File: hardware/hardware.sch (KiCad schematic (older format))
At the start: 12 parts

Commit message: wip: power supply
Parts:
- added C? (x3): CP, symbol Device:CP
- added C? (x5): C, symbol Device:C
- added J?: Conn_01x02_Male, symbol Connector:Conn_01x02_Male
- added K?: HE721C0500, DIP952W51P254L1905H550Q14N, symbol HE721C0500:HE721C0500
- added L? (x2): L, symbol Device:L
- added Q?: BC107, Package_TO_SOT_THT:TO-18-3, symbol Transistor_BJT:BC107
- added SW?: Trk next, symbol Switch:SW_Push
- added SW?: Trk prev, symbol Switch:SW_Push
- added SW?: Vol up, symbol Switch:SW_Push
- added SW?: Vol down, symbol Switch:SW_Push
- added SW?: SW_Push, symbol Switch:SW_Push
- added U?: TLV1117-33, symbol Regulator_Linear:TLV1117-33
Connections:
- net labels added: +3.3V, CTS, DTR
- wire segments 90 -> 132
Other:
- moved on the sheet: J?, R?, U?

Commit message: wip: power switch and cleanup
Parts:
- added D? (x2): D, symbol Device:D
- added R? (x2): 10k, symbol Device:R
- J?: value Conn_01x02_Male -> Power
- SW?: value SW_Push -> Power
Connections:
- net labels added: POWER_CTRL, RFID-MISO, RFID-MOSI, RFID-RST, RFID-SCK, RFID-SDA, SD-CS, SD-MISO, SD-MOSI, SD-SCK, SW_POWER, TRK_NEXT, TRK_PREV, VOL_DOWN, VOL_UP
- net labels removed: CS, GND, MISO, MOSI, RST, SDA, VIN
- wire segments 132 -> 116
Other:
- moved on the sheet: C?, J?, K?, Q?, R?, SW?, U?

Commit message: fix power switch circuit
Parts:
- added D? (x4): D, symbol Device:D
- added Q?: BC107, Package_TO_SOT_THT:TO-18-3, symbol Transistor_BJT:BC107
- added R? (x3): 10k, symbol Device:R
- added R?: 220, symbol Device:R
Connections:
- wire segments 116 -> 130
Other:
- moved on the sheet: C?, D?, J?, Q?, R?, SW?, U?

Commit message: update schematics
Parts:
- removed C? (x2): CP, symbol Device:CP
- removed D? (x5): D, symbol Device:D
- removed J?: Power, symbol Connector:Conn_01x02_Male
- removed L?: L, symbol Device:L
- removed Q?: BC107, Package_TO_SOT_THT:TO-18-3, symbol Transistor_BJT:BC107
- removed R? (x5): 10k, symbol Device:R
- removed SW?: Power, symbol Switch:SW_Push
- added C? (x2): 4.7uF, symbol Device:C
- added C?: C, symbol Device:C
- added J?: Power, symbol Connector:Conn_01x03_Male
- added R?: 150k, symbol Device:R
- added R?: 390k, symbol Device:R
- added U?: XRP6272, symbol XRP6272:XRP6272
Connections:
- wire segments 130 -> 123
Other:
- moved on the sheet: Q?, R?

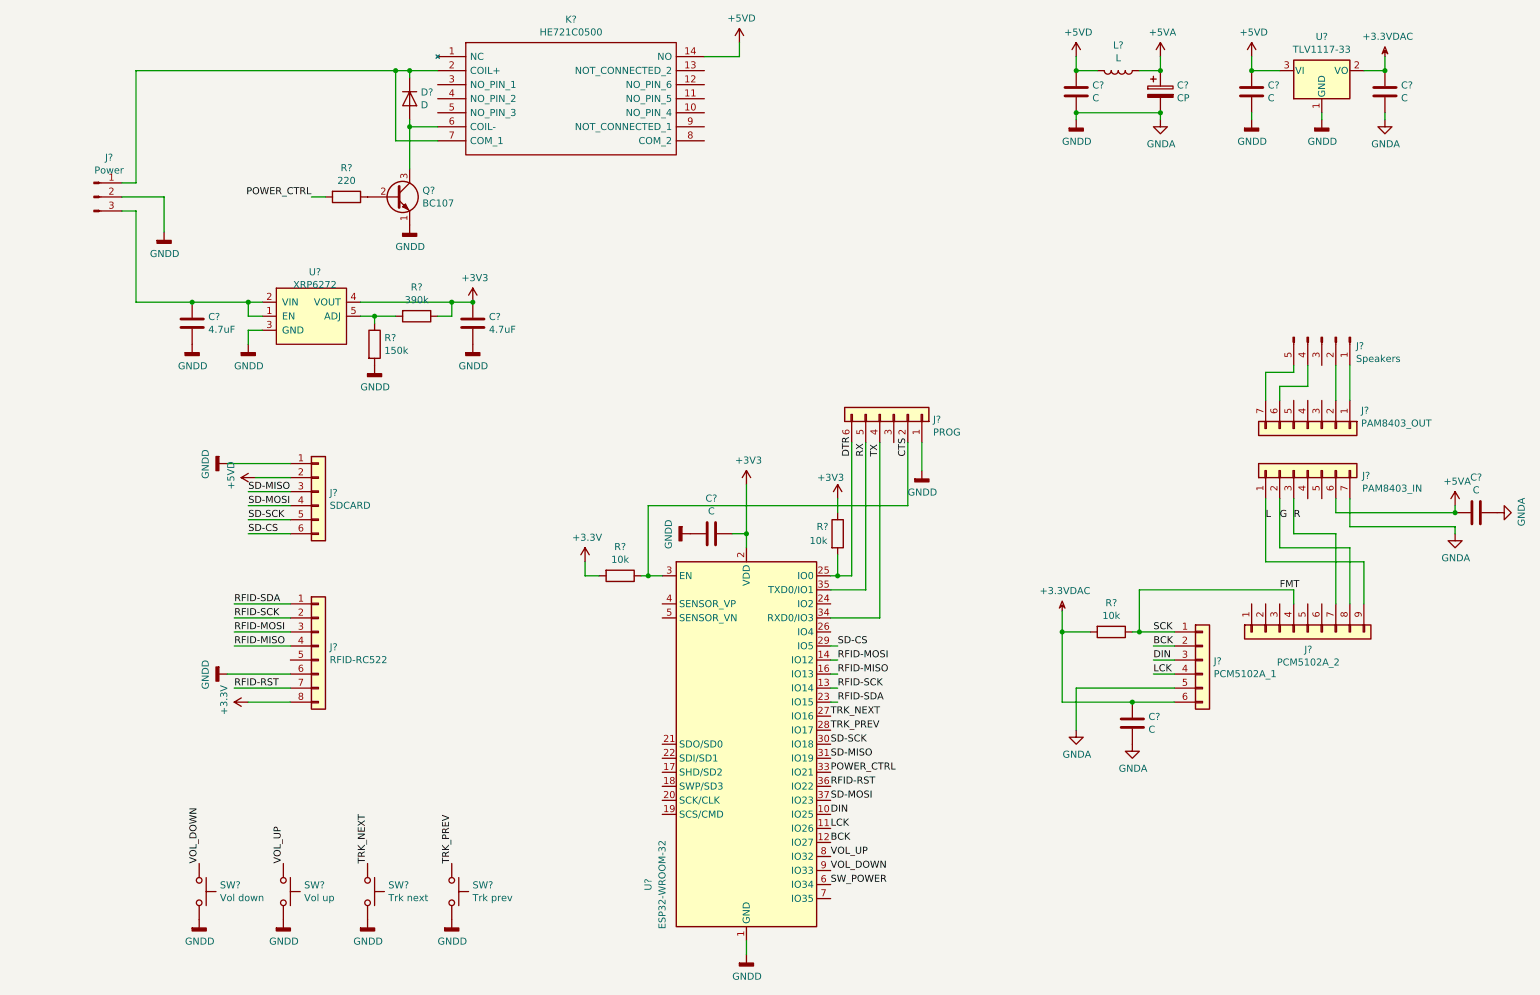
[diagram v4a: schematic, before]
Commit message: update schematics, improve power distribution concept
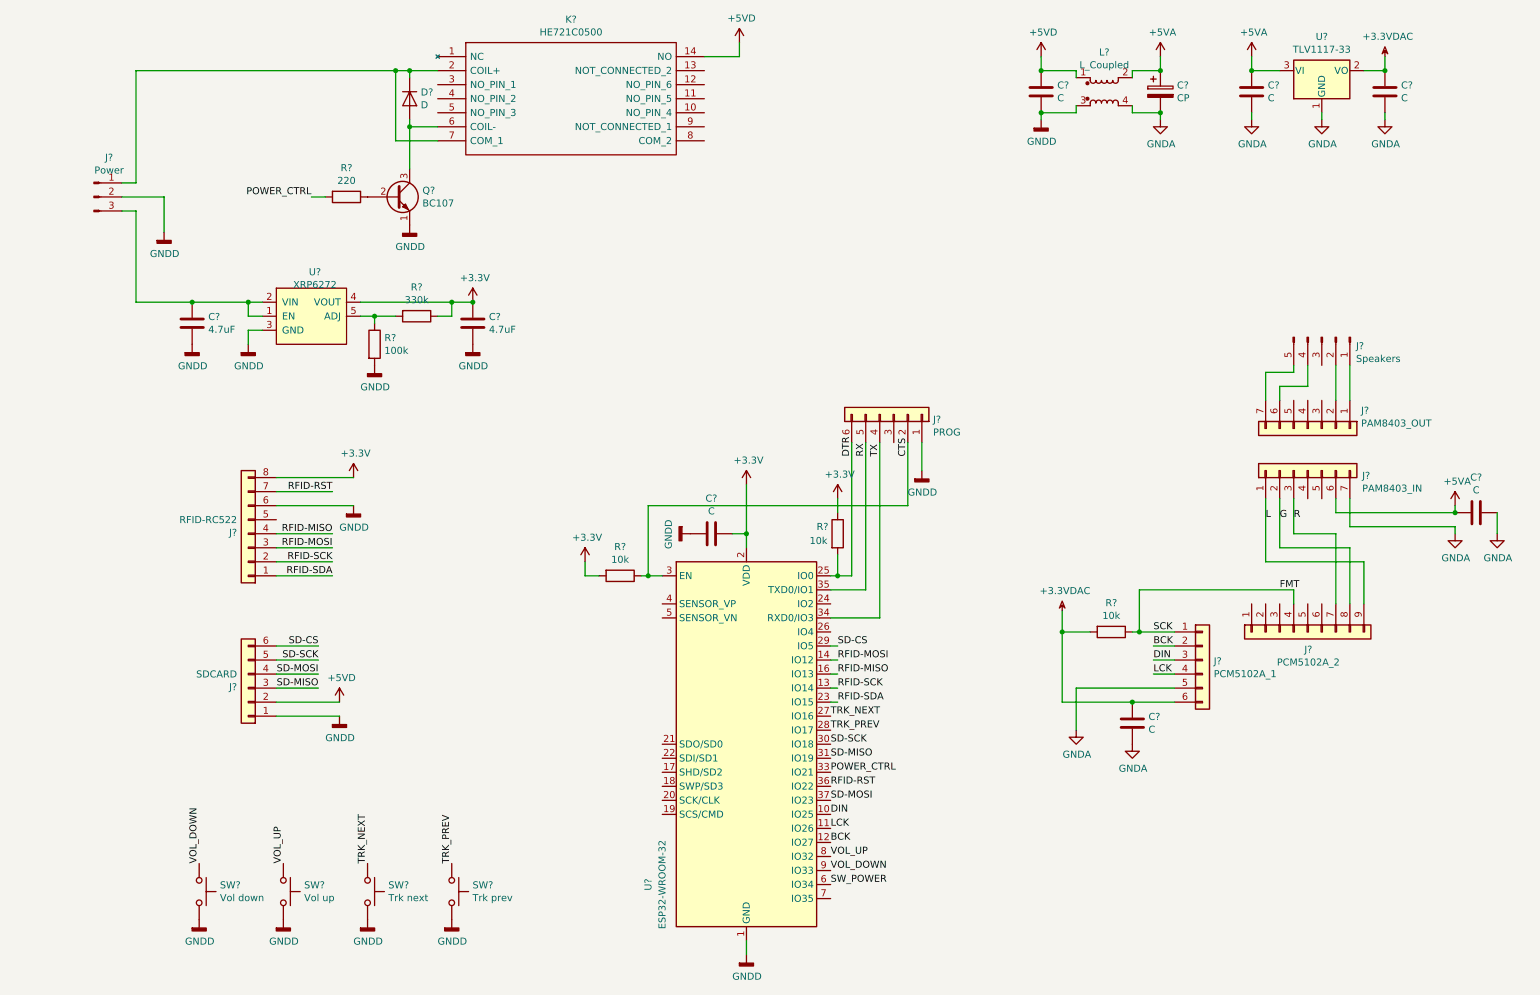
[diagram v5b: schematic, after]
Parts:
- removed L?: L, symbol Device:L
- added L?: L_Coupled, symbol Device:L_Coupled
- R?: value 150k -> 100k
- R?: value 390k -> 330k
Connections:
- net +5VA: now also C?.1, U?.3 (VI), L?.2
- net +5VD: now also L?.1; no longer C?.1, U?.3 (VI)
- net GNDA: now also L?.4; no longer C?.2, C?.2, C?.2, C?.2, J?.1 (Pin_1), J?.1 (Pin_1), J?.2 (Pin_2), J?.6 (Pin_6), Q?.1 (E), R?.2, SW?.2, SW?.2, SW?.2, SW?.2, U?.1 (GND), U?.15 (GND), U?.3 (GND), U?.38 (GND)
- new net GNDD: C?.2, C?.2, C?.2, C?.2, J?.1 (Pin_1), J?.1 (Pin_1), J?.2 (Pin_2), J?.6 (Pin_6), L?.3, Q?.1 (E), R?.2, SW?.2, SW?.2, SW?.2, SW?.2, U?.1 (GND), U?.15 (GND), U?.3 (GND), U?.38 (GND)
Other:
- moved on the sheet: C?, J?

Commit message: some fixes to the schematics
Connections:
- net RFID-MOSI: now also U?.23 (IO15); no longer U?.14 (IO12)
- net RFID-RST: now also U?.24 (IO2); no longer U?.36 (IO22)
- net RFID-SCK: now also U?.14 (IO12); no longer U?.13 (IO14)
- net RFID-SDA: now also U?.26 (IO4); no longer U?.23 (IO15)
- net CTS renamed RTS
- net SW_POWER: no longer names the net of U?.6 (IO34)
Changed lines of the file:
@@
 DTR
 Text Label 6400 3750 1    50   ~ 0
-CTS
+RTS
 $Comp
 L Switch:SW_Push SW?
@@
 	2850 1400 2850 1350
 Connection ~ 2850 1400
-Text Label 5900 5500 0    50   ~ 0
+Text Label 5850 5000 0    50   ~ 0
 RFID-SDA
-Text Label 5900 5400 0    50   ~ 0
+Text Label 5850 5200 0    50   ~ 0
 RFID-SCK
-Text Label 5900 5200 0    50   ~ 0
+Text Label 5850 5500 0    50   ~ 0
 RFID-MOSI
-Text Label 5900 5300 0    50   ~ 0
+Text Label 5850 5300 0    50   ~ 0
 RFID-MISO
-Wire Wire Line
-	5850 5300 5900 5300
-Wire Wire Line
-	5850 5400 5900 5400
-Wire Wire Line
-	5850 5500 5900 5500
-Wire Wire Line
-	5850 5200 5900 5200
-Text Label 5850 6100 0    50   ~ 0
+Text Label 5850 4800 0    50   ~ 0
 RFID-RST
 Text Label 5850 5900 0    50   ~ 0
@@
 Text Label 5850 5800 0    50   ~ 0
 SD-SCK
-Text Label 5900 5100 0    50   ~ 0
-SD-CS
-Wire Wire Line
-	5850 5100 5900 5100
 Text Label 1350 6650 1    50   ~ 0
 VOL_DOWN
@@
 Text Label 5850 6500 0    50   ~ 0
 BCK
-Text Label 5850 6800 0    50   ~ 0
-SW_POWER
 Text Label 2150 1900 2    50   ~ 0
 POWER_CTRL
@@
 	1    0    0    -1
 $EndComp
+Text Label 5850 5100 0    50   ~ 0
+SD-CS
 $EndSCHEMATC
